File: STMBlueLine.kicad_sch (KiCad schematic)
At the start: 0 parts

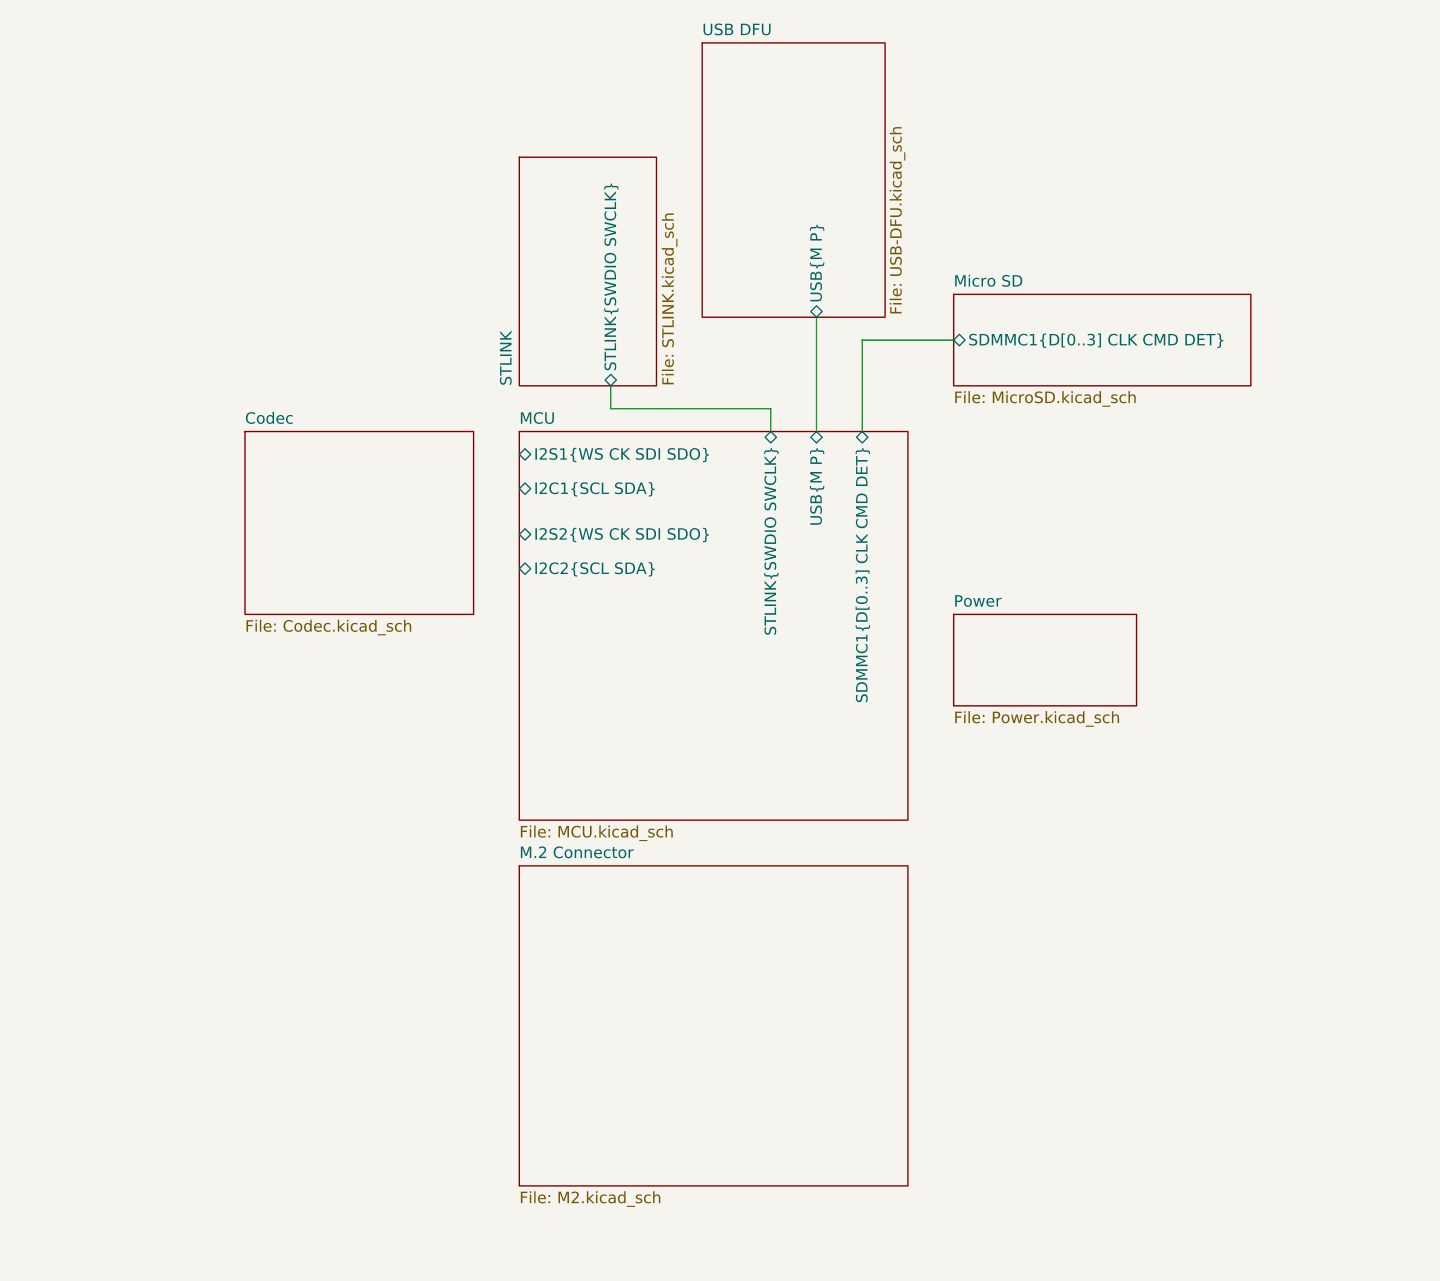
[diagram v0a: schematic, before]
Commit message: MOD : KiCad 8.0.1 -> 9.0.0. ADD : Codec power circuitry.
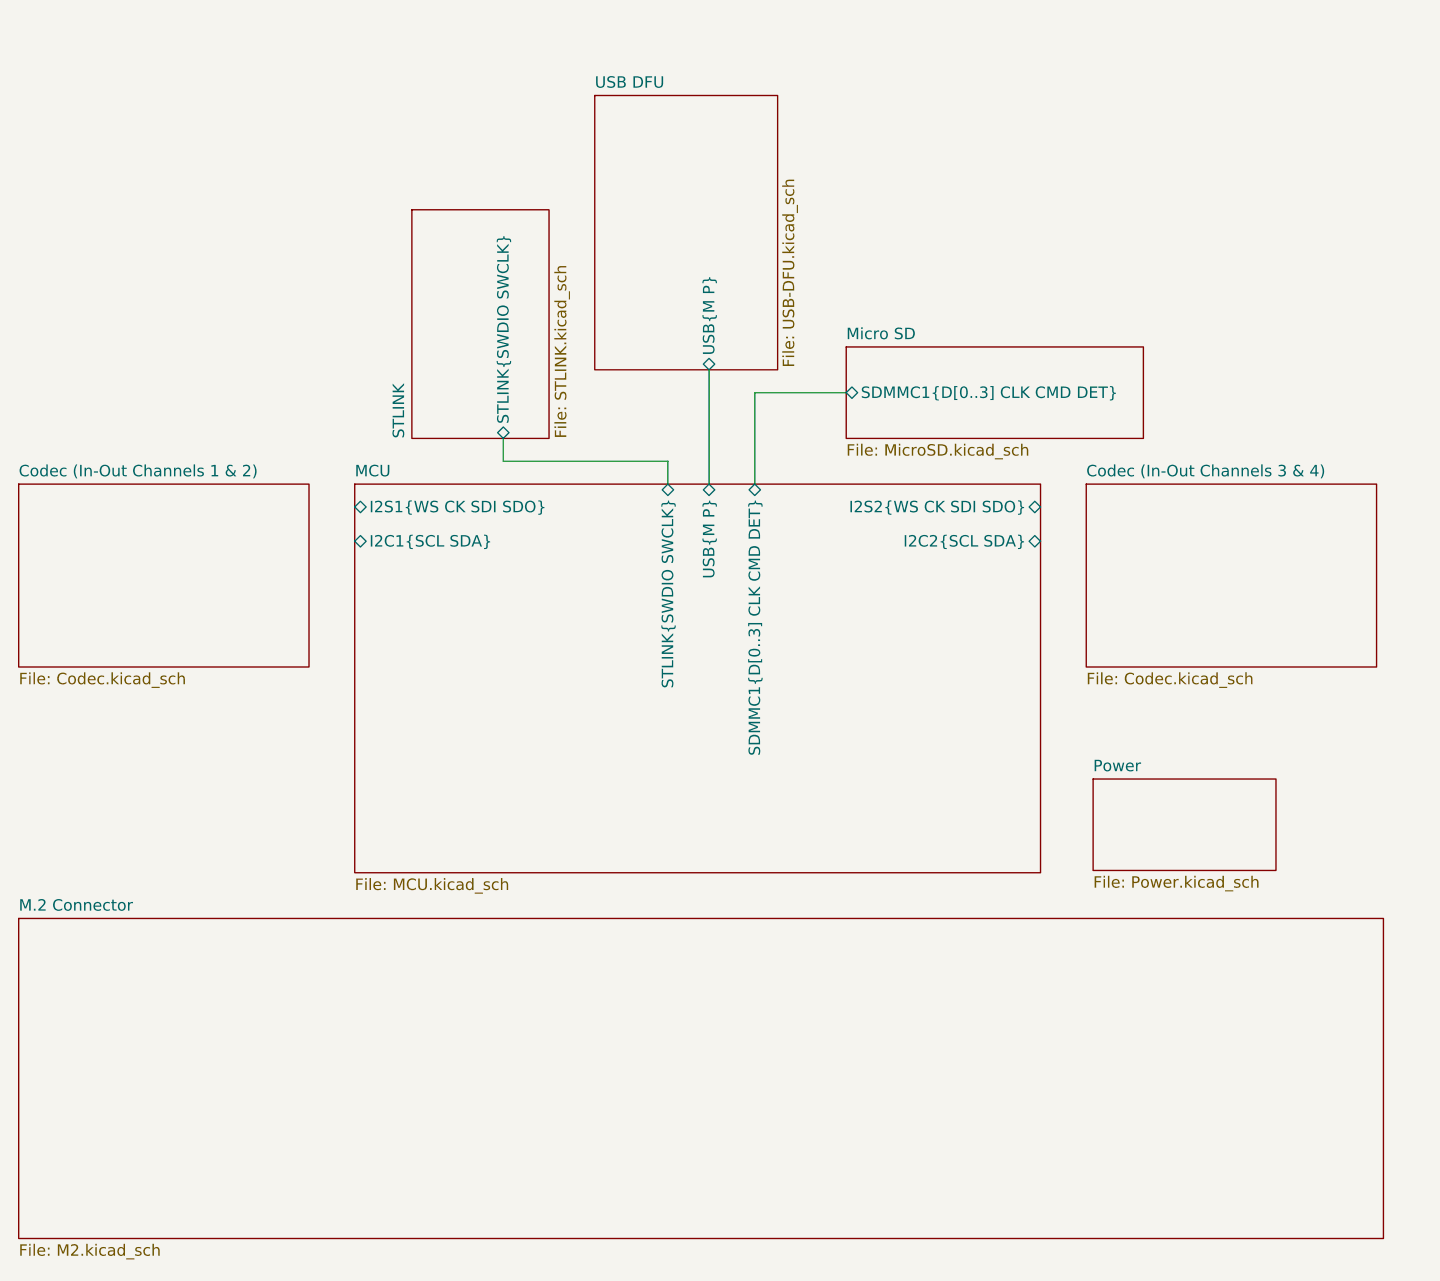
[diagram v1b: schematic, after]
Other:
- sheet Codec renamed Codec (In-Out Channels 1 & 2)
- added sheet Codec (In-Out Channels 3 & 4) (Codec.kicad_sch)

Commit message: ADD : Finished codec power and data connections
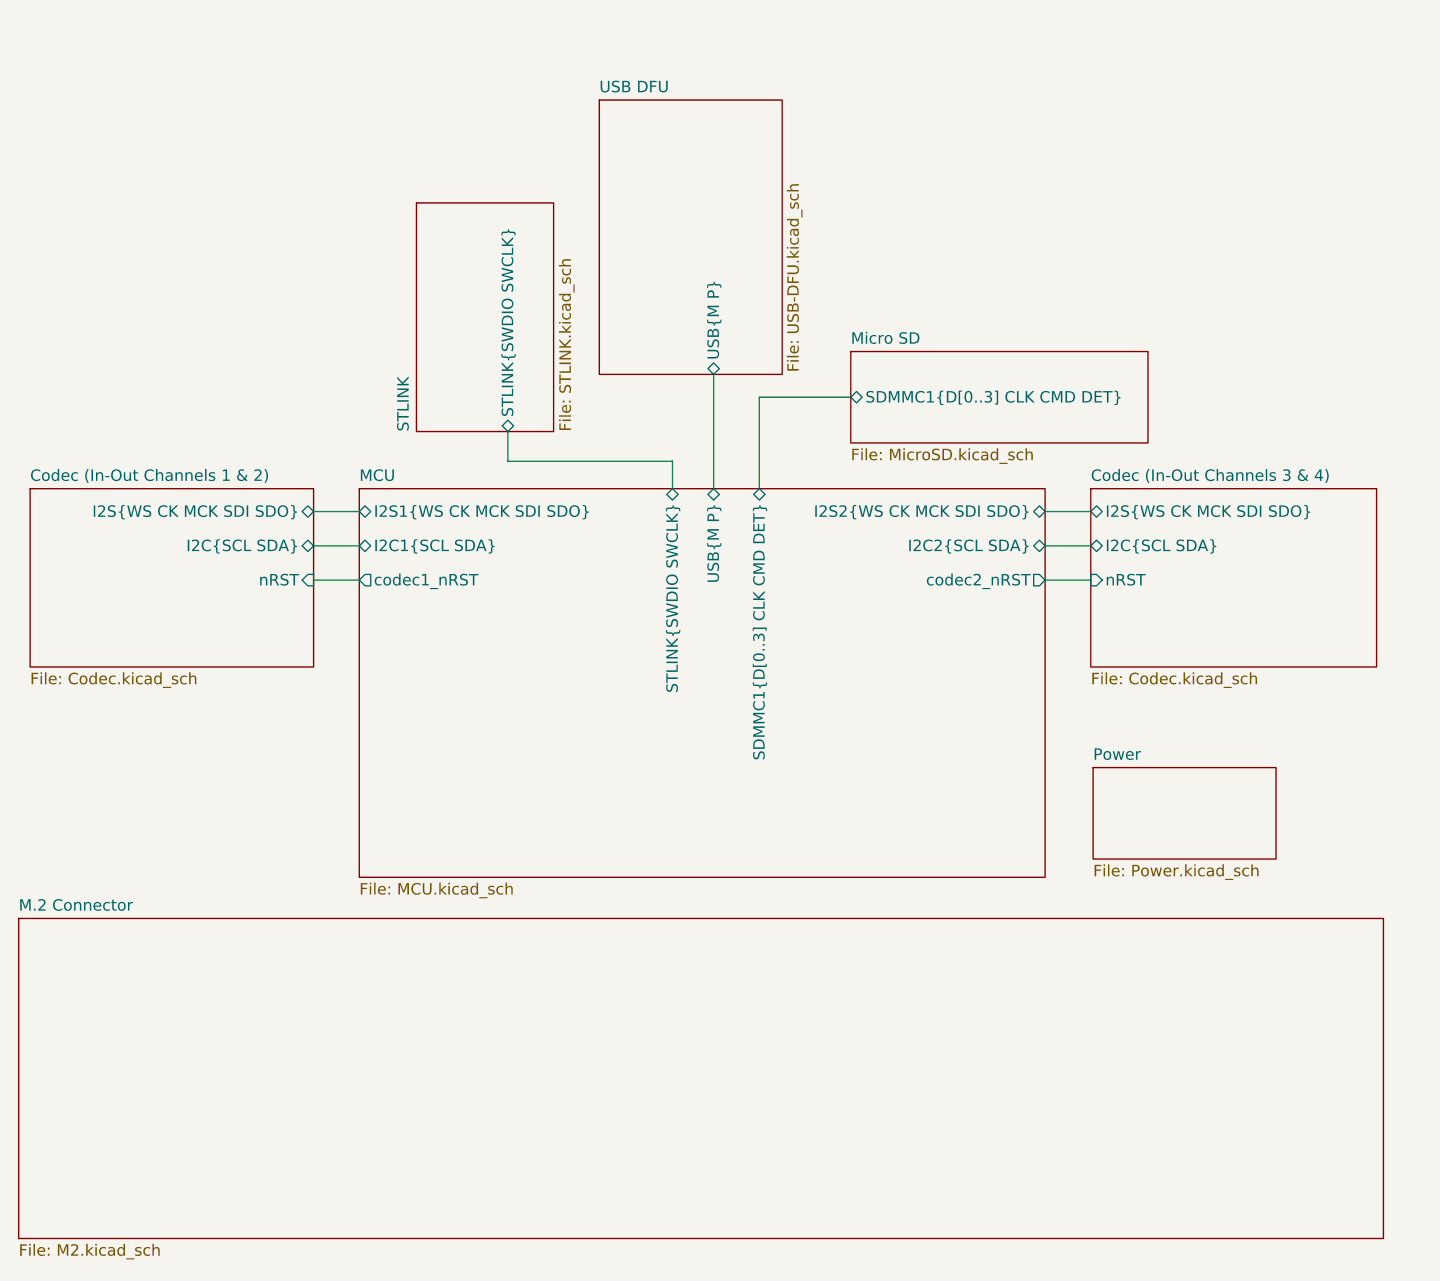
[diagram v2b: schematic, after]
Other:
- sheet Codec (In-Out Channels 1 & 2) ports: added I2C{SCL SDA}, I2S{WS CK MCK SDI SDO}, nRST; removed none
- sheet Codec (In-Out Channels 3 & 4) ports: added I2C{SCL SDA}, I2S{WS CK MCK SDI SDO}, nRST; removed none
- sheet MCU ports: added I2S1{WS CK MCK SDI SDO}, I2S2{WS CK MCK SDI SDO}, codec1_nRST, codec2_nRST; removed I2S1{WS CK SDI SDO}, I2S2{WS CK SDI SDO}

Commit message: ADD : Footprint assignment. FIX : Various ERC rules.
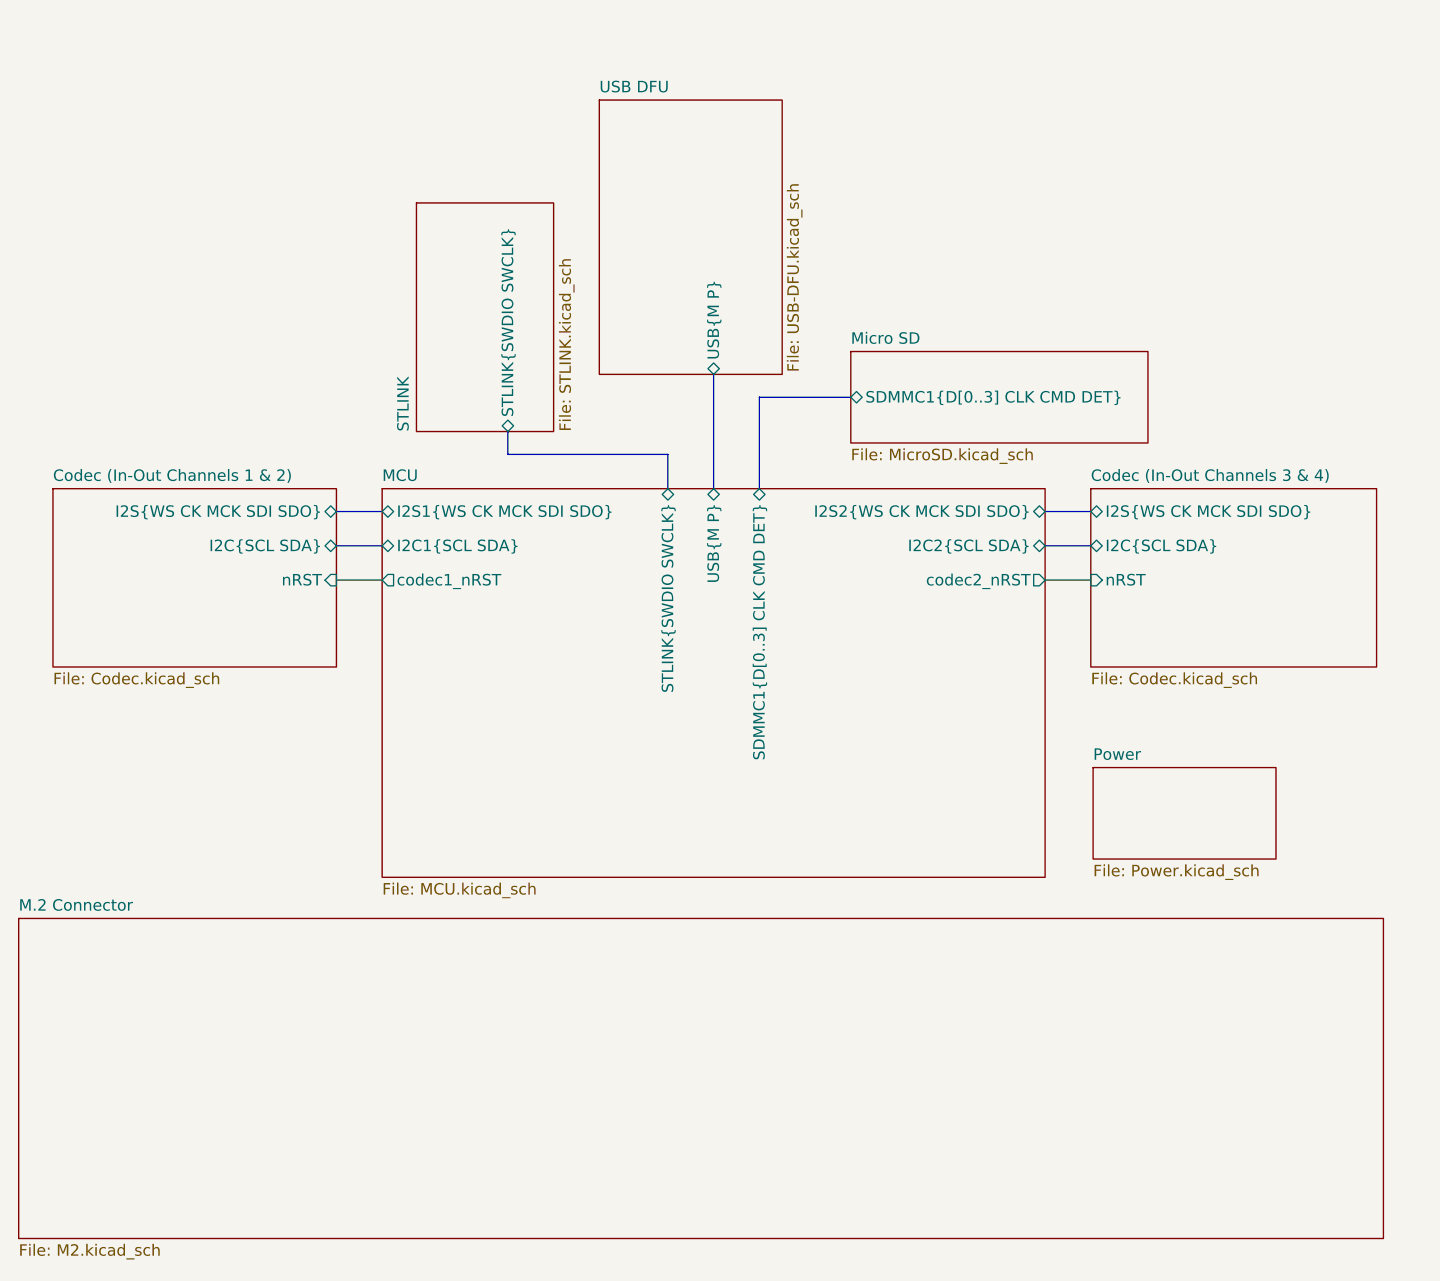
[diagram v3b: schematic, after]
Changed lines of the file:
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@@
 	(generator_version "9.0")
 	(paper "A4")
+	(bus
+		(pts
+			(xy 158.75 64.77) (xy 158.75 74.93)
+		)
+		(stroke
+			(width 0)
+			(type default)
+		)
+	)
+	(bus
+		(pts
+			(xy 111.76 77.47) (xy 116.84 77.47)
+		)
+		(stroke
+			(width 0)
+			(type default)
+		)
+	)
 	(wire
 		(pts
+			(xy 111.76 85.09) (xy 116.84 85.09)
+		)
+		(stroke
+			(width 0)
+			(type default)
+		)
+	)
+	(bus
+		(pts
+			(xy 158.75 64.77) (xy 168.91 64.77)
+		)
+		(stroke
+			(width 0)
+			(type default)
+		)
+	)
+	(wire
+		(pts
+			(xy 190.5 85.09) (xy 195.58 85.09)
+		)
+		(stroke
+			(width 0)
+			(type default)
+		)
+	)
+	(bus
+		(pts
+			(xy 130.81 68.58) (xy 130.81 71.12)
+		)
+		(stroke
+			(width 0)
+			(type default)
+		)
+	)
+	(bus
+		(pts
+			(xy 130.81 71.12) (xy 148.59 71.12)
+		)
+		(stroke
+			(width 0)
+			(type default)
+		)
+	)
+	(bus
+		(pts
+			(xy 153.67 62.23) (xy 153.67 74.93)
+		)
+		(stroke
+			(width 0)
+			(type default)
+		)
+	)
+	(bus
+		(pts
 			(xy 190.5 77.47) (xy 195.58 77.47)
 		)
@@
 		)
 	)
-	(wire
-		(pts
-			(xy 149.098 71.882) (xy 149.098 74.93)
-		)
-		(stroke
-			(width 0)
-			(type default)
-		)
-	)
-	(wire
+	(bus
+		(pts
+			(xy 111.76 81.28) (xy 116.84 81.28)
+		)
+		(stroke
+			(width 0)
+			(type default)
+		)
+	)
+	(bus
+		(pts
+			(xy 148.59 71.12) (xy 148.59 74.93)
+		)
+		(stroke
+			(width 0)
+			(type default)
+		)
+	)
+	(bus
 		(pts
 			(xy 190.5 81.28) (xy 195.58 81.28)
@@
 		)
 	)
-	(wire
-		(pts
-			(xy 109.22 85.09) (xy 114.3 85.09)
-		)
-		(stroke
-			(width 0)
-			(type default)
-		)
-	)
-	(wire
-		(pts
-			(xy 130.81 71.882) (xy 149.098 71.882)
-		)
-		(stroke
-			(width 0)
-			(type default)
-		)
-	)
-	(wire
-		(pts
-			(xy 158.75 64.77) (xy 158.75 74.93)
-		)
-		(stroke
-			(width 0)
-			(type default)
-		)
-	)
-	(wire
-		(pts
-			(xy 190.5 85.09) (xy 195.58 85.09)
-		)
-		(stroke
-			(width 0)
-			(type default)
-		)
-	)
-	(wire
-		(pts
-			(xy 130.81 68.58) (xy 130.81 71.882)
-		)
-		(stroke
-			(width 0)
-			(type default)
-		)
-	)
-	(wire
-		(pts
-			(xy 109.22 81.28) (xy 114.3 81.28)
-		)
-		(stroke
-			(width 0)
-			(type default)
-		)
-	)
-	(wire
-		(pts
-			(xy 109.22 77.47) (xy 114.3 77.47)
-		)
-		(stroke
-			(width 0)
-			(type default)
-		)
-	)
-	(wire
-		(pts
-			(xy 158.75 64.77) (xy 168.91 64.77)
-		)
-		(stroke
-			(width 0)
-			(type default)
-		)
-	)
-	(wire
-		(pts
-			(xy 153.67 62.23) (xy 153.67 74.93)
-		)
-		(stroke
-			(width 0)
-			(type default)
-		)
-	)
-	(sheet
-		(at 114.3 74.93)
-		(size 76.2 43.18)
+	(sheet
+		(at 116.84 74.93)
+		(size 73.66 43.18)
 		(exclude_from_sim no)
 		(in_bom yes)
@@
 		)
 		(property "Sheetname" "MCU"
-			(at 114.3 74.2184 0)
+			(at 116.84 74.2184 0)
 			(effects
 				(font
@@
 		)
 		(property "Sheetfile" "MCU.kicad_sch"
-			(at 114.3 118.6946 0)
+			(at 116.84 118.6946 0)
 			(effects
 				(font
@@
 		)
 		(pin "I2C1{SCL SDA}" bidirectional
-			(at 114.3 81.28 180)
+			(at 116.84 81.28 180)
 			(effects
 				(font
@@
 		)
 		(pin "STLINK{SWDIO SWCLK}" bidirectional
-			(at 149.098 74.93 90)
+			(at 148.59 74.93 90)
 			(effects
 				(font
@@
 		)
 		(pin "I2S1{WS CK MCK SDI SDO}" bidirectional
-			(at 114.3 77.47 180)
+			(at 116.84 77.47 180)
 			(effects
 				(font
@@
 		)
 		(pin "codec1_nRST" output
-			(at 114.3 85.09 180)
+			(at 116.84 85.09 180)
 			(effects
 				(font
@@
 	)
 	(sheet
-		(at 77.724 74.93)
+		(at 80.264 74.93)
 		(size 31.496 19.812)
 		(exclude_from_sim no)
@@
 		)
 		(property "Sheetname" "Codec (In-Out Channels 1 & 2)"
-			(at 77.724 74.2184 0)
+			(at 80.264 74.2184 0)
 			(effects
 				(font
@@
 		)
 		(property "Sheetfile" "Codec.kicad_sch"
-			(at 77.724 95.3266 0)
+			(at 80.264 95.3266 0)
 			(effects
 				(font
@@
 		)
 		(pin "nRST" input
-			(at 109.22 85.09 0)
+			(at 111.76 85.09 0)
 			(effects
 				(font
@@
 		)
 		(pin "I2C{SCL SDA}" bidirectional
-			(at 109.22 81.28 0)
+			(at 111.76 81.28 0)
 			(effects
 				(font
@@
 		)
 		(pin "I2S{WS CK MCK SDI SDO}" bidirectional
-			(at 109.22 77.47 0)
-			(effects
-				(font
+			(at 111.76 77.47 0)
+			(effects
+				(font
